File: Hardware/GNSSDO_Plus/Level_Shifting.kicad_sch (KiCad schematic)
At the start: 37 parts, among them J3 SMA_Edge, SW4 DPDT_Slide_SMD_7.2x3.5mm, U10 74LVC2T45DC, U12 74LVC2T45DC, U14 74LVC2T45DC, U8 74LVC2T45DC, U9 74LVC2T45DC

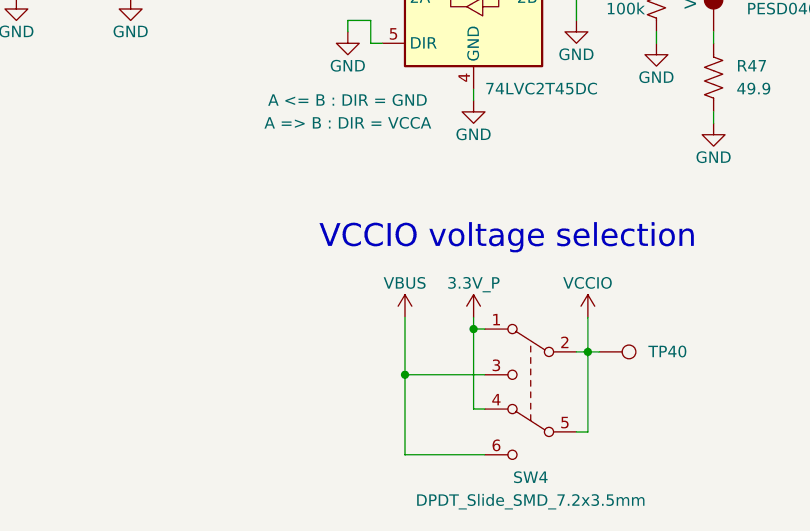
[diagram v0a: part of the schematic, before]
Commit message: GNSSDO Plus: add 3-way splitter
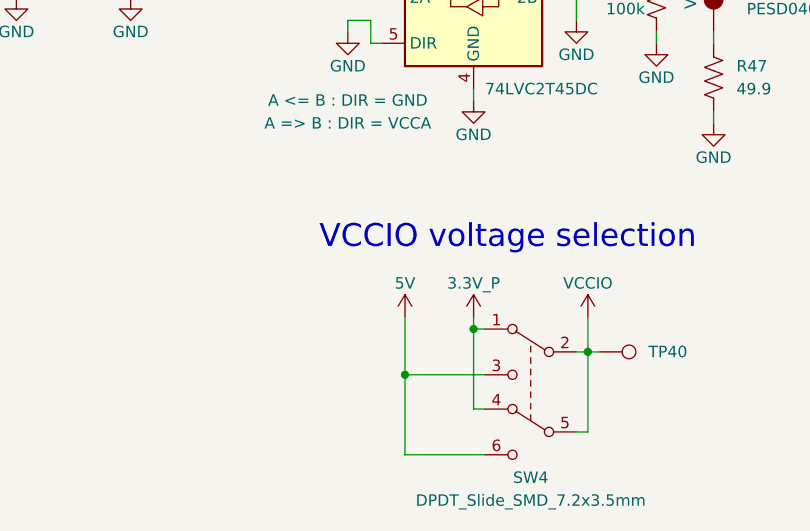
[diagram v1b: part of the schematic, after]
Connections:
- net VBUS renamed 5V
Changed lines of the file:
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@@
 	)
 	(symbol
-		(lib_id "SparkFun-PowerSymbol:VBUS")
-		(at 64.77 179.07 0)
-		(unit 1)
-		(exclude_from_sim no)
-		(in_bom yes)
-		(on_board yes)
-		(dnp no)
-		(fields_autoplaced yes)
-		(property "Reference" "#PWR0281"
-			(at 64.77 182.88 0)
-			(effects
-				(font
-					(size 1.27 1.27)
-				)
-				(hide yes)
-			)
-		)
-		(property "Value" "VBUS"
-			(at 64.77 175.26 0)
-			(do_not_autoplace yes)
-			(effects
-				(font
-					(size 1.27 1.27)
-				)
-			)
-		)
-		(property "Footprint" ""
-			(at 64.77 179.07 0)
-			(effects
-				(font
-					(size 1.27 1.27)
-				)
-				(hide yes)
-			)
-		)
-		(property "Datasheet" ""
-			(at 64.77 179.07 0)
-			(effects
-				(font
-					(size 1.27 1.27)
-				)
-				(hide yes)
-			)
-		)
-		(property "Description" "Power symbol creates a global label with name \"VBUS\""
-			(at 64.77 185.42 0)
-			(effects
-				(font
-					(size 1.27 1.27)
-				)
-				(hide yes)
-			)
-		)
-		(pin "1"
-		)
-		(instances
-			(project "SparkPNT_GNSSDO_Plus"
-				(path "/e3dd3ae4-244d-4cba-9cca-5d2abf83f29a/d9a77ac1-2999-4329-b708-8e6cc1b00c22"
-					(reference "#PWR0281")
-					(unit 1)
-				)
-			)
-		)
-	)
-	(symbol
 		(lib_id "SparkFun-DiscreteSemi:D_TVS_ESD_4_HS")
 		(at 106.68 52.07 90)
@@
 					(unit 1)
 				)
+			)
+		)
+	)
+	(symbol
+		(lib_id "SparkFun-PowerSymbol:5V")
+		(at 64.77 179.07 0)
+		(unit 1)
+		(exclude_from_sim no)
+		(in_bom yes)
+		(on_board yes)
+		(dnp no)
+		(fields_autoplaced yes)
+		(property "Reference" "#PWR0169"
+			(at 64.77 182.88 0)
+			(effects
+				(font
+					(size 1.27 1.27)
+				)
+				(hide yes)
+			)
+		)
+		(property "Value" "5V"
+			(at 64.77 175.26 0)
+			(do_not_autoplace yes)
+			(effects
+				(font
+					(size 1.27 1.27)
+				)
+			)
+		)
+		(property "Footprint" ""
+			(at 64.77 179.07 0)
+			(effects
+				(font
+					(size 1.27 1.27)
+				)
+				(hide yes)
+			)
+		)
+		(property "Datasheet" ""
+			(at 64.77 179.07 0)
+			(effects
+				(font
+					(size 1.27 1.27)
+				)
+				(hide yes)
+			)
+		)
+		(property "Description" "Power symbol creates a global label with name \"5V\""
+			(at 64.77 179.07 0)
+			(effects
+				(font
+					(size 1.27 1.27)
+				)
+				(hide yes)
+			)
+		)
+		(pin "1"
+		)
+		(instances
+			(project "SparkPNT_GNSSDO_Plus"
+				(path "/e3dd3ae4-244d-4cba-9cca-5d2abf83f29a/d9a77ac1-2999-4329-b708-8e6cc1b00c22"
+					(reference "#PWR0169")
+					(unit 1)
+				)

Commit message: GNSSDO+ WIP
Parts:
- removed TP20: PTH, SparkFun-Connector:1x01, symbol SparkFun-Connector:TestPoint_PTH
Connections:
- net MGP1_O: now also D14.1 (K1); no longer D14.5 (K4)
- net MGP2_O: now reaches U14.6 (2B)
- net MGP2_O: now also D14.5 (K4)
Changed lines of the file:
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@@
 	(wire
 		(pts
-			(xy 214.63 57.15) (xy 215.9 57.15)
+			(xy 92.71 128.27) (xy 92.71 127)
 		)
 		(stroke
@@
 	(wire
 		(pts
-			(xy 92.71 128.27) (xy 92.71 127)
+			(xy 85.09 67.31) (xy 90.17 67.31)
 		)
 		(stroke
@@
 	(wire
 		(pts
-			(xy 85.09 67.31) (xy 90.17 67.31)
+			(xy 168.91 146.05) (xy 168.91 144.78)
 		)
 		(stroke
@@
 	(wire
 		(pts
-			(xy 168.91 146.05) (xy 168.91 144.78)
+			(xy 34.29 49.53) (xy 34.29 48.26)
 		)
 		(stroke
@@
 	(wire
 		(pts
-			(xy 34.29 49.53) (xy 34.29 48.26)
+			(xy 97.79 71.12) (xy 102.87 71.12)
 		)
 		(stroke
@@
 	(wire
 		(pts
-			(xy 97.79 71.12) (xy 102.87 71.12)
+			(xy 214.63 57.15) (xy 215.9 57.15)
 		)
 		(stroke
@@
 	(wire
 		(pts
+			(xy 240.03 128.27) (xy 241.3 128.27)
+		)
+		(stroke
+			(width 0)
+			(type default)
+		)
+	)
+	(wire
+		(pts
 			(xy 168.91 62.23) (xy 168.91 60.96)
 		)
@@
 		)
 	)
-	(text "I/O Screw Terminal"
+	(text "I/O Screw Terminals"
 		(exclude_from_sim no)
-		(at 237.49 53.34 0)
+		(at 238.76 54.61 0)
 		(effects
 			(font
@@
 		)
 	)
+	(global_label "MGP1_O"
+		(shape input)
+		(at 240.03 128.27 180)
+		(fields_autoplaced yes)
+		(effects
+			(font
+				(size 1.27 1.27)
+			)
+			(justify right)
+		)
+		(property "Intersheetrefs" "${INTERSHEET_REFS}"
+			(at 229.5458 128.27 0)
+			(effects
+				(font
+					(size 1.27 1.27)
+				)
+				(justify right)
+				(hide yes)
+			)
+		)
+	)
 	(global_label "MEventB_I"
 		(shape input)
@@
 		)
 	)
+	(global_label "MGP2_O"
+		(shape input)
+		(at 215.9 57.15 0)
+		(fields_autoplaced yes)
+		(effects
+			(font
+				(size 1.27 1.27)
+			)
+			(justify left)
+		)
+		(property "Intersheetrefs" "${INTERSHEET_REFS}"
+			(at 226.3842 57.15 0)
+			(effects
+				(font
+					(size 1.27 1.27)
+				)
+				(justify left)
+				(hide yes)
+			)
+		)
+	)
 	(global_label "MRTS2_O"
 		(shape input)
@@
 		)
 	)
-	(global_label "MGP1_O"
+	(global_label "MGP2_O"
 		(shape input)
 		(at 240.03 120.65 180)
@@
 					(unit 1)
 				)
-			)
-		)
-	)
-	(symbol
-		(lib_id "SparkFun-Connector:TestPoint_PTH")
-		(at 215.9 57.15 270)
-		(mirror x)
-		(unit 1)
-		(exclude_from_sim no)
-		(in_bom yes)
-		(on_board yes)
-		(dnp no)
-		(fields_autoplaced yes)
-		(property "Reference" "TP20"
-			(at 220.98 57.1499 90)
-			(effects
-				(font
-					(size 1.27 1.27)
-				)
-				(justify left)
-			)
-		)
-		(property "Value" "PTH"
-			(at 212.09 57.15 0)
-			(effects
-				(font
-					(size 1.27 1.27)
-				)
-				(hide yes)
-			)
-		)
-		(property "Footprint" "SparkFun-Connector:1x01"
-			(at 209.55 58.42 0)
-			(effects
-				(font
-					(size 1.27 1.27)
-				)
-				(hide yes)
-			)
-		)
-		(property "Datasheet" "~"
-			(at 208.28 57.15 0)
-			(effects
-				(font
-					(size 1.27 1.27)
-				)
-				(hide yes)
-			)
-		)
-		(property "Description" "Test Point"
-			(at 215.9 57.15 0)
-			(effects
-				(font
-					(size 1.27 1.27)
-				)
-				(hide yes)
-			)
-		)
-		(pin "1"
-		)
-		(instances
-			(project "SparkPNT_GNSSDO_Plus"
-				(path "/e3dd3ae4-244d-4cba-9cca-5d2abf83f29a/d9a77ac1-2999-4329-b708-8e6cc1b00c22"
-					(reference "TP20")
-					(unit 1)
-				)

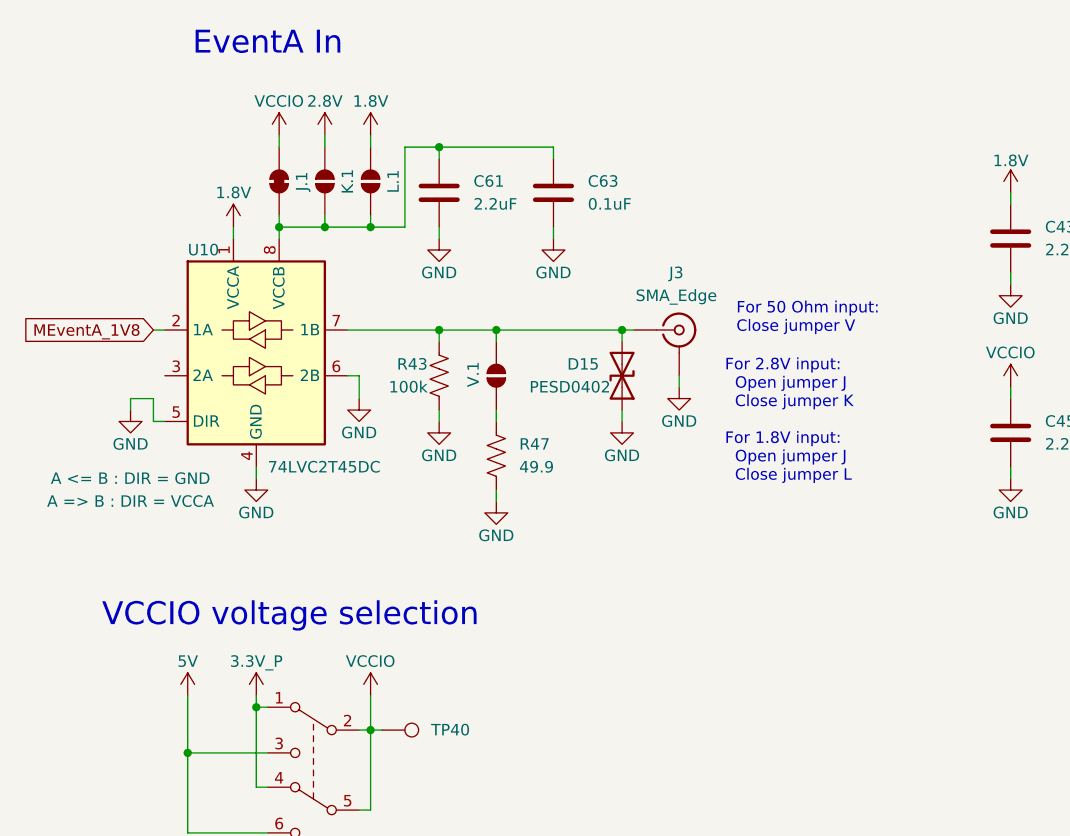
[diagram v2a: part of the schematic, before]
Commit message: GNSSDO+ routed
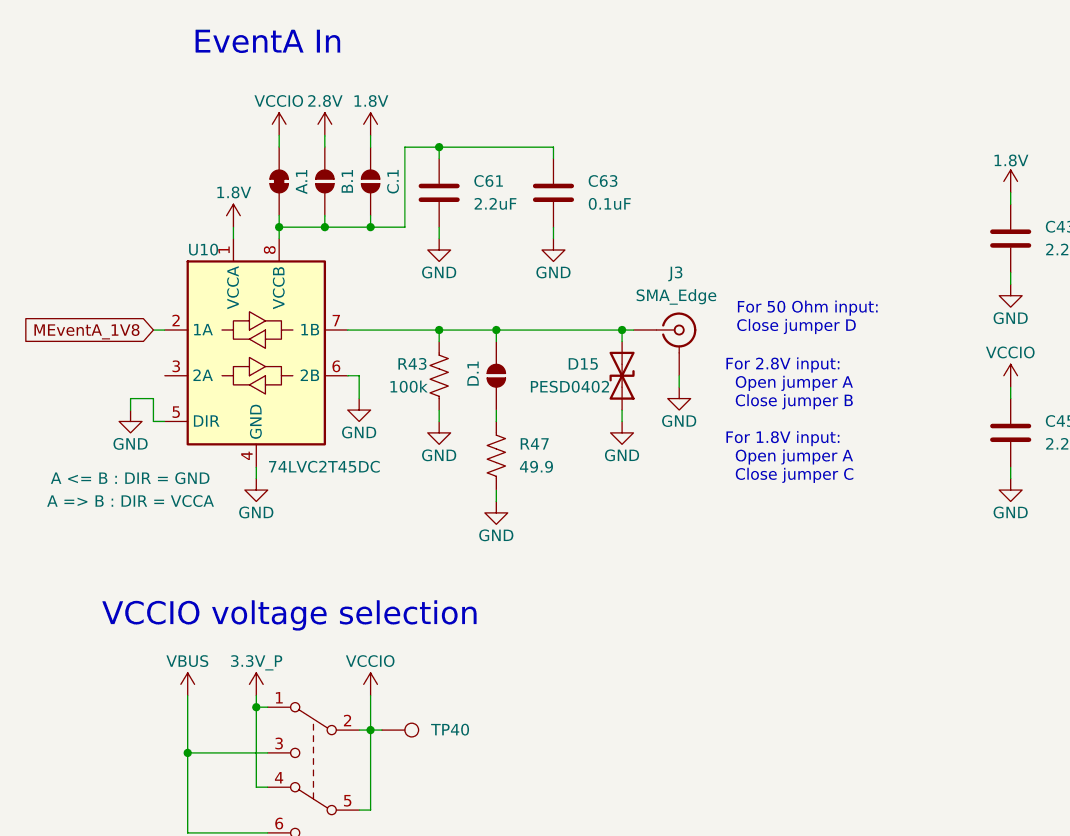
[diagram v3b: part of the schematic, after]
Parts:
- renumbered J.1 to A.1, K.1 to B.1, L.1 to C.1, V.1 to D.1
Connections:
- net 5V renamed VBUS
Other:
- note added: "For 2.8V input: Open jumper A Close jumper B For 1.8V input: Open jumper A Close jumper C"
- note added: "For 50 Ohm input: Close jumper D"
- note removed: "For 2.8V input: Open jumper J Close jumper K For 1.8V input: Open jumper J Close jumper L"
- note removed: "For 50 Ohm input: Close jumper V"
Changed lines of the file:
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@@
 		)
 	)
-	(text "For 50 Ohm input:\nClose jumper V"
+	(text "For 50 Ohm input:\nClose jumper D"
 		(exclude_from_sim no)
 		(at 125.73 137.16 0)
@@
 		)
 	)
-	(text "For 2.8V input:\n  Open jumper J\n  Close jumper K\n\nFor 1.8V input:\n  Open jumper J\n  Close jumper L"
+	(text "For 2.8V input:\n  Open jumper A\n  Close jumper B\n\nFor 1.8V input:\n  Open jumper A\n  Close jumper C"
 		(exclude_from_sim no)
 		(at 124.46 148.59 0)
@@
 		(on_board yes)
 		(dnp no)
-		(property "Reference" "V.1"
+		(property "Reference" "D.1"
 			(at 96.52 144.78 0)
 			(effects
@@
 			(project "SparkFun_RTK_mosaic-T"
 				(path "/e3dd3ae4-244d-4cba-9cca-5d2abf83f29a/d9a77ac1-2999-4329-b708-8e6cc1b00c22"
-					(reference "V.1")
+					(reference "D.1")
 					(unit 1)
 				)
@@
 	)
 	(symbol
+		(lib_id "SparkFun-PowerSymbol:VBUS")
+		(at 64.77 179.07 0)
+		(unit 1)
+		(exclude_from_sim no)
+		(in_bom yes)
+		(on_board yes)
+		(dnp no)
+		(fields_autoplaced yes)
+		(property "Reference" "#PWR0169"
+			(at 64.77 182.88 0)
+			(effects
+				(font
+					(size 1.27 1.27)
+				)
+				(hide yes)
+			)
+		)
+		(property "Value" "VBUS"
+			(at 64.77 175.26 0)
+			(do_not_autoplace yes)
+			(effects
+				(font
+					(size 1.27 1.27)
+				)
+			)
+		)
+		(property "Footprint" ""
+			(at 64.77 179.07 0)
+			(effects
+				(font
+					(size 1.27 1.27)
+				)
+				(hide yes)
+			)
+		)
+		(property "Datasheet" ""
+			(at 64.77 179.07 0)
+			(effects
+				(font
+					(size 1.27 1.27)
+				)
+				(hide yes)
+			)
+		)
+		(property "Description" "Power symbol creates a global label with name \"VBUS\""
+			(at 64.77 185.42 0)
+			(effects
+				(font
+					(size 1.27 1.27)
+				)
+				(hide yes)
+			)
+		)
+		(pin "1"
+		)
+		(instances
+			(project "SparkPNT_GNSSDO_Plus"
+				(path "/e3dd3ae4-244d-4cba-9cca-5d2abf83f29a/d9a77ac1-2999-4329-b708-8e6cc1b00c22"
+					(reference "#PWR0169")
+					(unit 1)
+				)
+			)
+		)
+	)
+	(symbol
 		(lib_id "SparkFun-DiscreteSemi:D_TVS_ESD_4_HS")
 		(at 245.11 125.73 90)
@@
 		(on_board yes)
 		(dnp no)
-		(property "Reference" "J.1"
+		(property "Reference" "A.1"
 			(at 77.47 121.92 0)
 			(effects
@@
 			(project "SparkFun_RTK_mosaic-T"
 				(path "/e3dd3ae4-244d-4cba-9cca-5d2abf83f29a/d9a77ac1-2999-4329-b708-8e6cc1b00c22"
-					(reference "J.1")
+					(reference "A.1")
 					(unit 1)
 				)
@@
 		(on_board yes)
 		(dnp no)
-		(property "Reference" "K.1"
+		(property "Reference" "B.1"
 			(at 82.55 121.92 0)
 			(effects
@@
 			(project "SparkFun_RTK_mosaic-T"
 				(path "/e3dd3ae4-244d-4cba-9cca-5d2abf83f29a/d9a77ac1-2999-4329-b708-8e6cc1b00c22"
-					(reference "K.1")
+					(reference "B.1")
 					(unit 1)
 				)
@@
 	)
 	(symbol
-		(lib_id "SparkFun-PowerSymbol:5V")
-		(at 64.77 179.07 0)
-		(unit 1)
-		(exclude_from_sim no)
-		(in_bom yes)
-		(on_board yes)
-		(dnp no)
-		(fields_autoplaced yes)
-		(property "Reference" "#PWR0169"
-			(at 64.77 182.88 0)
-			(effects
-				(font
-					(size 1.27 1.27)
-				)
-				(hide yes)
-			)
-		)
-		(property "Value" "5V"
-			(at 64.77 175.26 0)
-			(do_not_autoplace yes)
-			(effects
-				(font
-					(size 1.27 1.27)
-				)
-			)
-		)
-		(property "Footprint" ""
-			(at 64.77 179.07 0)
-			(effects
-				(font
-					(size 1.27 1.27)
-				)
-				(hide yes)
-			)
-		)
-		(property "Datasheet" ""
-			(at 64.77 179.07 0)
-			(effects
-				(font
-					(size 1.27 1.27)
-				)
-				(hide yes)
-			)
-		)
-		(property "Description" "Power symbol creates a global label with name \"5V\""
-			(at 64.77 179.07 0)
-			(effects
-				(font
-					(size 1.27 1.27)
-				)
-				(hide yes)
-			)
-		)
-		(pin "1"
-		)
-		(instances
-			(project "SparkPNT_GNSSDO_Plus"
-				(path "/e3dd3ae4-244d-4cba-9cca-5d2abf83f29a/d9a77ac1-2999-4329-b708-8e6cc1b00c22"
-					(reference "#PWR0169")
-					(unit 1)
-				)
-			)
-		)
-	)
-	(symbol
 		(lib_id "SparkFun-Jumper:SolderJumper_2_Open")
 		(at 85.09 121.92 90)
@@
 		(on_board yes)
 		(dnp no)
-		(property "Reference" "L.1"
+		(property "Reference" "C.1"
 			(at 87.63 121.92 0)
 			(effects
@@
 			(project "SparkFun_RTK_mosaic-T"
 				(path "/e3dd3ae4-244d-4cba-9cca-5d2abf83f29a/d9a77ac1-2999-4329-b708-8e6cc1b00c22"
-					(reference "L.1")
+					(reference "C.1")
 					(unit 1)
 				)
